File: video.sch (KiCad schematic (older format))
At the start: 62 parts, among them IC114 AY38912, IC115 AMS40464, J102 audio/video, J103 Jack audio, Q103 KTC1815Y, Q104 KTC1815Y, Q105 KTC1815Y, Q106 KTC1815Y, Q107 KTC1815Y

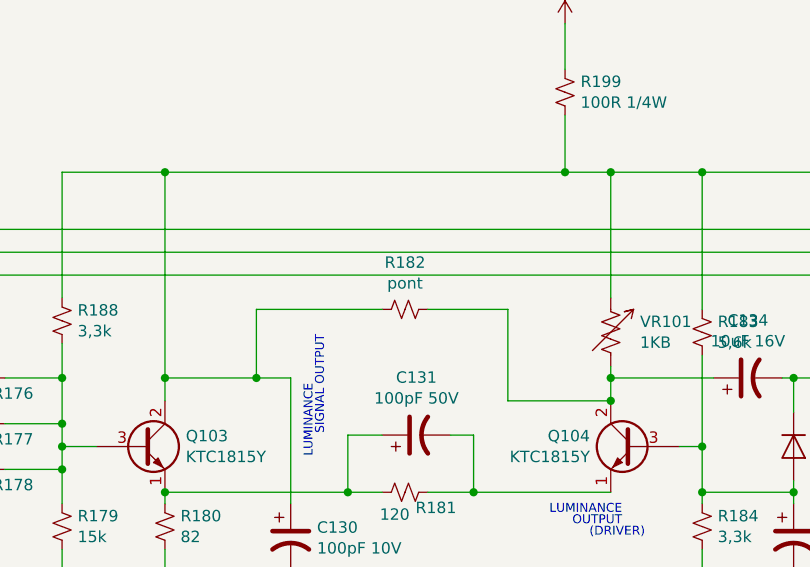
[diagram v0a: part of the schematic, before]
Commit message: more accurate on pins definition, power, centronic 36, jack, and some wiring
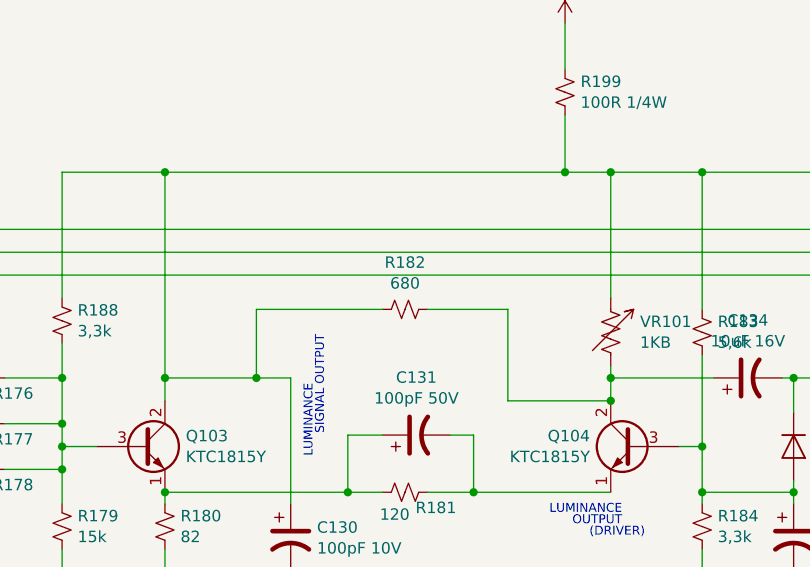
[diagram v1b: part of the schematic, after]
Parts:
- C130: footprint Capacitor_THT:CP_Radial_D8.0mm_P2.50mm -> Capacitor_THT:CP_Radial_D8.0mm_P5.00mm
- C135: footprint Capacitor_THT:CP_Radial_D5.0mm_P2.50mm -> Capacitor_THT:CP_Radial_D8.0mm_P5.00mm
- C151: footprint (none) -> Capacitor_THT:CP_Radial_D5.0mm_P2.50mm
- IC114: footprint Package_DIP:DIP-28_W7.62mm -> Package_DIP:DIP-28_W15.24mm
- J103: footprint Connector_Audio:Jack_3.5mm_CUI_SJ1-3533NG_Horizontal -> cpc6128+:Jack_6128
- R182: value pont -> 680
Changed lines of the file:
@@
 F 0 "J103" H 10320 5526 50  0000 R CNN
 F 1 "Jack audio" H 10320 5617 50  0000 R CNN
-F 2 "Connector_Audio:Jack_3.5mm_CUI_SJ1-3533NG_Horizontal" H 10500 5600 50  0001 C CNN
+F 2 "cpc6128+:Jack_6128" H 10500 5600 50  0001 C CNN
 F 3 "~" H 10500 5600 50  0001 C CNN
 	1    10500 5600
@@
 F 0 "IC114" H 3750 7331 50  0000 C CNN
 F 1 "AY38912" H 3750 7240 50  0000 C CNN
-F 2 "Package_DIP:DIP-28_W7.62mm" H 3750 6200 50  0001 C CNN
+F 2 "Package_DIP:DIP-28_W15.24mm" H 3750 6200 50  0001 C CNN
 F 3 "" H 3750 6200 50  0001 C CNN
 	1    3750 6200
@@
 F 0 "C130" H 5915 3296 50  0000 L CNN
 F 1 "100pF 10V" H 5915 3205 50  0000 L CNN
-F 2 "Capacitor_THT:CP_Radial_D8.0mm_P2.50mm" H 5800 3250 50  0001 C CNN
+F 2 "Capacitor_THT:CP_Radial_D8.0mm_P5.00mm" H 5800 3250 50  0001 C CNN
 F 3 "~" H 5800 3250 50  0001 C CNN
 	1    5800 3250
@@
 F 0 "C151" H 9115 2396 50  0000 L CNN
 F 1 "47uF 16V" H 9115 2305 50  0000 L CNN
-F 2 "" H 9000 2350 50  0001 C CNN
+F 2 "Capacitor_THT:CP_Radial_D5.0mm_P2.50mm" H 9000 2350 50  0001 C CNN
 F 3 "~" H 9000 2350 50  0001 C CNN
 	1    9000 2350
@@
 F 0 "C135" H 3165 1196 50  0000 L CNN
 F 1 "100uF 10V" H 3165 1105 50  0000 L CNN
-F 2 "Capacitor_THT:CP_Radial_D5.0mm_P2.50mm" H 3050 1150 50  0001 C CNN
+F 2 "Capacitor_THT:CP_Radial_D8.0mm_P5.00mm" H 3050 1150 50  0001 C CNN
 F 3 "~" H 3050 1150 50  0001 C CNN
 	1    3050 1150
@@
 P 6300 2250
 F 0 "R182" V 6095 2250 50  0000 C CNN
-F 1 "pont" V 6186 2250 50  0000 C CNN
+F 1 "680" V 6186 2250 50  0000 C CNN
 F 2 "Resistor_THT:R_Axial_DIN0204_L3.6mm_D1.6mm_P5.08mm_Horizontal" H 6300 2250 50  0001 C CNN
 F 3 "~" H 6300 2250 50  0001 C CNN

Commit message: finished the centronic 36, some more refinements on placement, new footprint for some connectors
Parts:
- CP103: footprint Connector_PinSocket_1.27mm:PinSocket_1x10_P1.27mm_Vertical -> cpc6128+:CP_103_104
- CP104: value Conn 10 -> clavier; footprint Connector_PinSocket_1.27mm:PinSocket_1x10_P1.27mm_Vertical -> cpc6128+:CP_103_104
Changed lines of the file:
@@
 Wire Wire Line
 	9000 2200 9000 1650
-Text Notes 9650 1350 2    39   ~ 0
+Text Notes 9700 1300 2    39   ~ 0
 KEYBOARD Y\nCP104\nHBLB105-5J
 Wire Wire Line
@@
 Text Label 10000 1550 2    39   ~ 0
 Y10
-Wire Bus Line
-	9100 1750 9750 1750
-Text Label 9450 1750 2    39   ~ 0
-Y[1..10]
 Wire Wire Line
 	3950 1900 9800 1900
@@
 P 10350 1050
 F 0 "CP104" H 10378 1026 50  0000 L CNN
-F 1 "Conn 10" H 10378 935 50  0000 L CNN
-F 2 "Connector_PinSocket_1.27mm:PinSocket_1x10_P1.27mm_Vertical" H 10350 1050 50  0001 C CNN
+F 1 "clavier" H 10378 935 50  0000 L CNN
+F 2 "cpc6128+:CP_103_104" H 10350 1050 50  0001 C CNN
 F 3 "~" H 10350 1050 50  0001 C CNN
 	1    10350 1050
@@
 F 0 "CP103" H 6378 6526 50  0000 L CNN
 F 1 "clavier" H 6378 6435 50  0000 L CNN
-F 2 "Connector_PinSocket_1.27mm:PinSocket_1x10_P1.27mm_Vertical" H 6350 6550 50  0001 C CNN
+F 2 "cpc6128+:CP_103_104" H 6350 6550 50  0001 C CNN
 F 3 "~" H 6350 6550 50  0001 C CNN
 	1    6350 6550
@@
 Wire Bus Line
 	2850 6150 2500 6150
-Text Label 2500 6150 0    50   ~ 0
-PA[0..7]
 Text Label 3000 6250 0    50   ~ 0
 PA0
@@
 Entry Wire Line
 	1950 7350 2050 7450
-Text Label 950  7450 0    50   ~ 0
-X[1..8]
 $Comp
 L power:+5V #PWR0133
@@
 Wire Wire Line
 	5250 2550 5650 2550
+Text GLabel 9550 1750 0    39   Input ~ 0
+Y[1..10]
+Wire Bus Line
+	9550 1750 9750 1750
+Text GLabel 950  7450 0    39   Input ~ 0
+X[1..8]
 Wire Bus Line
 	2850 6150 2850 6850
@@
 Wire Bus Line
 	950  7450 5500 7450
+Text GLabel 2500 6150 0    39   Input ~ 0
+PA[0..7]
 $EndSCHEMATC

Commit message: Cabled the keyboard
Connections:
- net X1: now also NR102.9 (R8)
- net X2: now also NR102.8 (R7)
- net X3: now also NR102.7 (R6)
- net X4: now also NR102.6 (R5)
- net X5: now also NR102.5 (R4)
- net X6: now also NR102.4 (R3)
- net X7: now also NR102.3 (R2)
- net X8: now also NR102.2 (R1)
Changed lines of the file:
@@
 Text GLabel 950  7450 0    39   Input ~ 0
 X[1..8]
+Text GLabel 2500 6150 0    39   Input ~ 0
+PA[0..7]
+Text Label 1950 7250 1    39   ~ 0
+X1
+Text Label 1850 7250 1    39   ~ 0
+X2
+Text Label 1750 7250 1    39   ~ 0
+X3
+Text Label 1650 7250 1    39   ~ 0
+X4
+Text Label 1550 7250 1    39   ~ 0
+X5
+Text Label 1450 7250 1    39   ~ 0
+X6
+Text Label 1350 7250 1    39   ~ 0
+X7
+Text Label 1250 7250 1    39   ~ 0
+X8
 Wire Bus Line
 	2850 6150 2850 6850
@@
 Wire Bus Line
 	950  7450 5500 7450
-Text GLabel 2500 6150 0    39   Input ~ 0
-PA[0..7]
 $EndSCHEMATC

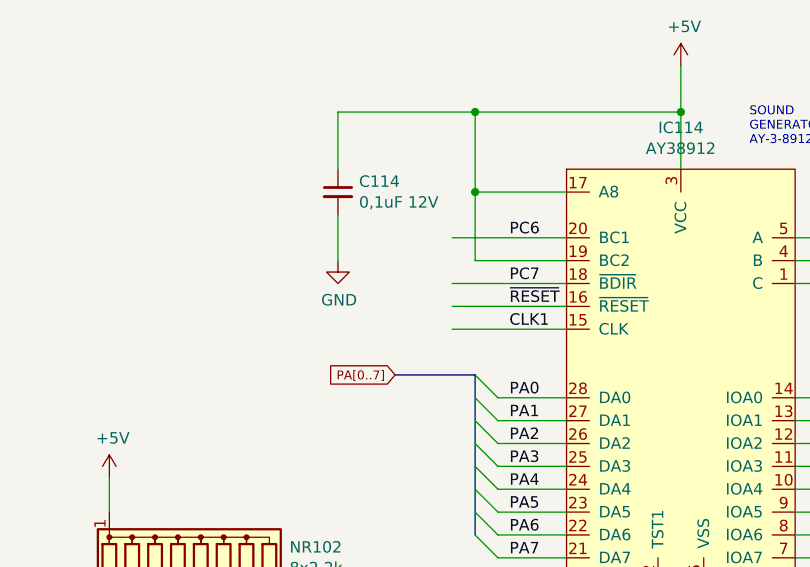
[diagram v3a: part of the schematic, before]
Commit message: 29-03-2021 : first usage of hierarchical labels. focus on CPU/ Cartridge Connector
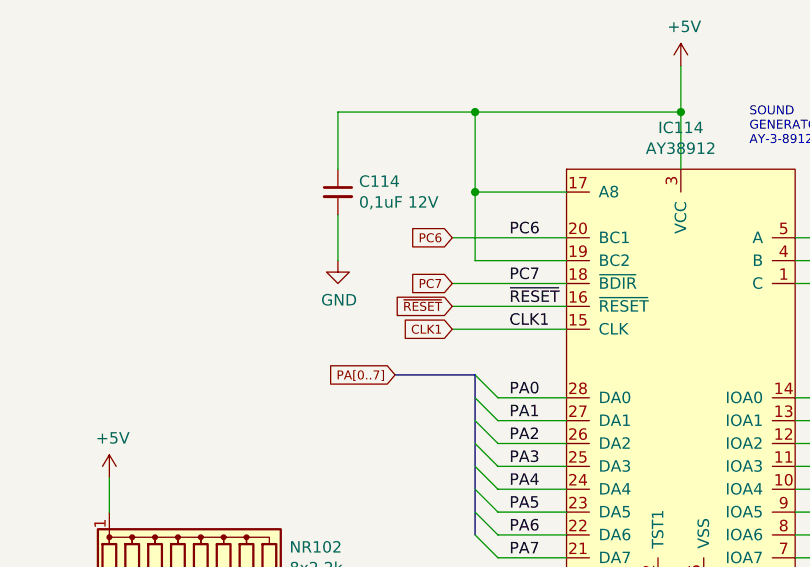
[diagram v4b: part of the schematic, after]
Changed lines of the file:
@@
 Text Label 1250 7250 1    39   ~ 0
 X8
+Text GLabel 2750 5550 0    39   Input ~ 0
+PC6
+Text GLabel 2750 5750 0    39   Input ~ 0
+PC7
+Text GLabel 2750 5850 0    39   Input ~ 0
+~RESET
+Text GLabel 2750 5950 0    39   Input ~ 0
+CLK1
 Wire Bus Line
 	2850 6150 2850 6850

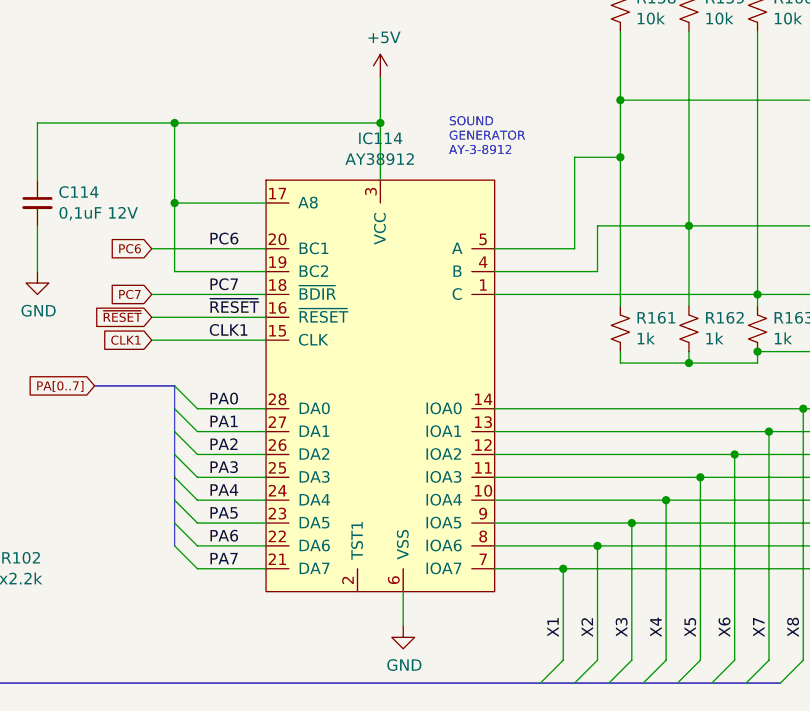
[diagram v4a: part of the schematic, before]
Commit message: work on sound chip : A,B,C & X8
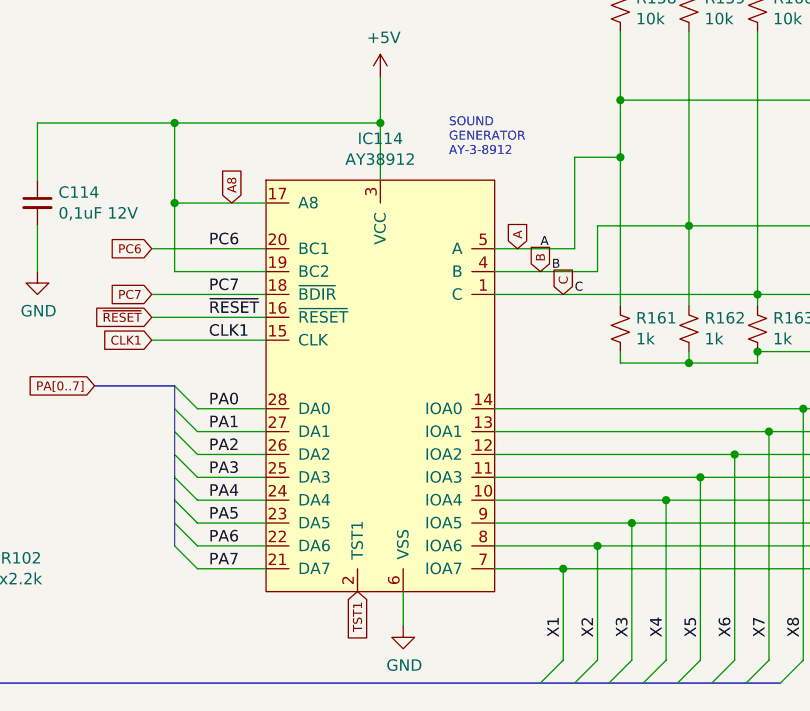
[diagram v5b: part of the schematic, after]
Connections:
- net C: now reaches IC114.1 (C), R160.2, R163.1, R167.1
- net TST1: now reaches IC114.2 (TST1)
- net B: now reaches IC114.4 (B), R159.2, R162.1, R165.1, R166.1
- net A: now reaches IC114.5 (A), R158.2, R161.1, R164.1
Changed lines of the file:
@@
 Text GLabel 2750 5950 0    39   Input ~ 0
 CLK1
+Text GLabel 3650 7050 3    39   Input ~ 0
+TST1
+Text GLabel 4350 5550 1    39   Input ~ 0
+A
+Text GLabel 4450 5650 1    39   Input ~ 0
+B
+Text GLabel 4550 5750 1    39   Input ~ 0
+C
 Wire Bus Line
 	2850 6150 2850 6850
@@
 Wire Bus Line
 	950  7450 5500 7450
+Text GLabel 3100 5350 1    39   Input ~ 0
+A8
+Text Label 4450 5550 0    39   ~ 0
+A
+Text Label 4500 5650 0    39   ~ 0
+B
+Text Label 4600 5750 0    39   ~ 0
+C
 $EndSCHEMATC

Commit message: Work on the sound Part, close to the Audio Jack. correction of Q_NPN_ECB
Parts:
- Q106, Q107: symbol Device:Q_NPN_BCE -> Device:Q_NPN_ECB
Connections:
- net L: now also J103.T, Q106.1 (E); no longer J103.S, Q106.3 (E)
- net R: now also J103.S, Q107.1 (E); no longer J103.T, Q107.3 (E)
- net at R196.2, R197.1: now also C138.1, Q107.3 (B); no longer C138.2, Q107.1 (B)
- net at R164.2, R165.2: now also C137.2; no longer C137.1
- net at R193.2, R194.1: now also C137.1, Q106.3 (B); no longer C137.2, Q106.1 (B)
- net at R166.2, R167.2: now also C138.2; no longer C138.1
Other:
- moved on the sheet: J103
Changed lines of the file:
@@
 	10150 4350 10150 4550
-$Comp
-L Device:Q_NPN_BCE Q107
-U 1 1 6080BE90
-P 9500 4700
-F 0 "Q107" H 9690 4738 50  0000 L CNN
-F 1 "KTC1815Y" H 9690 4655 39  0000 L CNN
-F 2 "Package_TO_SOT_THT:TO-92_Inline_Wide" H 9700 4800 50  0001 C CNN
-F 3 "~" H 9500 4700 50  0001 C CNN
-	1    9500 4700
-	1    0    0    -1
-$EndComp
 $Comp
 L Device:R_Small_US R198
@@
 L Connector:AudioJack2_Ground J103
 U 1 1 6082D566
-P 10500 5600
-F 0 "J103" H 10320 5526 50  0000 R CNN
-F 1 "Jack audio" H 10320 5617 50  0000 R CNN
-F 2 "cpc6128+:Jack_6128" H 10500 5600 50  0001 C CNN
-F 3 "~" H 10500 5600 50  0001 C CNN
-	1    10500 5600
-	-1   0    0    1
+P 10500 5700
+F 0 "J103" H 10320 5626 50  0000 R CNN
+F 1 "Jack audio" H 10320 5717 50  0000 R CNN
+F 2 "cpc6128+:Jack_6128" H 10500 5700 50  0001 C CNN
+F 3 "~" H 10500 5700 50  0001 C CNN
+	1    10500 5700
+	-1   0    0    -1
 $EndComp
 $Comp
 L power:GND #PWR0124
 U 1 1 608477C6
-P 10150 5350
-F 0 "#PWR0124" H 10150 5100 50  0001 C CNN
-F 1 "GND" H 10155 5177 50  0000 C CNN
-F 2 "" H 10150 5350 50  0001 C CNN
-F 3 "" H 10150 5350 50  0001 C CNN
-	1    10150 5350
-	1    0    0    -1
-$EndComp
-Wire Wire Line
-	10150 5350 10150 5250
-Wire Wire Line
-	10150 5250 10500 5250
-Wire Wire Line
-	10500 5250 10500 5400
+P 10150 6100
+F 0 "#PWR0124" H 10150 5850 50  0001 C CNN
+F 1 "GND" H 10155 5927 50  0000 C CNN
+F 2 "" H 10150 6100 50  0001 C CNN
+F 3 "" H 10150 6100 50  0001 C CNN
+	1    10150 6100
+	1    0    0    -1
+$EndComp
+Wire Wire Line
+	10150 6100 10150 6000
+Wire Wire Line
+	10150 6000 10500 6000
+Wire Wire Line
+	10500 5900 10500 6000
 $Comp
 L power:+5V #PWR0125
@@
 F 3 "~" H 7450 4700 50  0001 C CNN
 	1    7450 4700
-	0    -1   -1   0
+	0    1    -1   0
 $EndComp
 Wire Wire Line
@@
 $EndComp
 $Comp
-L Device:Q_NPN_BCE Q106
+L Device:Q_NPN_ECB Q106
 U 1 1 609A4624
 P 8100 4700
@@
 F 3 "~" H 8850 4700 50  0001 C CNN
 	1    8850 4700
-	0    -1   -1   0
+	0    1    -1   0
 $EndComp
 Wire Wire Line
@@
 Text GLabel 4550 5750 1    39   Input ~ 0
 C
-Wire Bus Line
-	2850 6150 2850 6850
-Wire Bus Line
-	9750 750  9750 1750
-Wire Bus Line
-	950  7450 5500 7450
 Text GLabel 3100 5350 1    39   Input ~ 0
 A8
@@
 Text Label 4600 5750 0    39   ~ 0
 C
+$Comp
+L Device:Q_NPN_ECB Q107
+U 1 1 6080BE90
+P 9500 4700
+F 0 "Q107" H 9690 4738 50  0000 L CNN
+F 1 "KTC1815Y" H 9690 4655 39  0000 L CNN
+F 2 "Package_TO_SOT_THT:TO-92_Inline_Wide" H 9700 4800 50  0001 C CNN
+F 3 "~" H 9500 4700 50  0001 C CNN
+	1    9500 4700
+	1    0    0    -1
+$EndComp
+Wire Bus Line
+	2850 6150 2850 6850
+Wire Bus Line
+	9750 750  9750 1750
+Wire Bus Line
+	950  7450 5500 7450
 $EndSCHEMATC
